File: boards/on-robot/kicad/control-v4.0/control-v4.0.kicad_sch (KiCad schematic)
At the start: 7 parts, among them IC1 MCP23017E_SS, J1 Conn_01x08_MountingPin, U1 Teensy4.1, U3 NRF24L01_Breakout

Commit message: 10/8
Update 10/8
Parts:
- removed J1: Conn_01x08_MountingPin, Connector_JST:JST_SH_SM08B-SRSS-TB_1x08-1MP_P1.00mm_Horizontal, symbol Connector_Generic_MountingPin:Conn_01x08_MountingPin
- added C1: 0.1 uF, Capacitor_SMD:CP_Elec_3x5.3, symbol Device:C_Small
- added J2, J3, J4, J5: 52901-0274, RoboJackets-Connectors:529010274, symbol 52901-0274:52901-0274
- R1: footprint (none) -> Resistor_SMD:R_0201_0603Metric
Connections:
- net RX_M3: now also U1.42 (20_A6_TX5_LRCLK1); no longer U1.36 (14_A0_TX3_SPDIF_OUT)
- net TX_M3: now also U1.43 (21_A7_RX5_BCLK1); no longer U1.37 (15_A1_RX3_SPDIF_IN)
- net GND: now reaches U3.1 (GND)
- net GND: now also IC1.10 (VSS), IC1.15 (A0), IC1.16 (A1), IC1.17 (A2), IC1.18 (/RESET), IC1.9 (VDD), S1.C1, S1.C2, U2.5 (GND), C1.2, J2.12, J2.14, J2.16, J2.18, J2.20, J3.12, J3.14, J3.16, J3.18, J3.20, J4.12, J4.14, J4.16, J4.18, J4.20, J5.12, J5.14, J5.16, J5.18, J5.20
- net +3.3V: now reaches U3.2 (VCC)
- net +3.3V: now also U2.4 (~{CS}), U2.8 (3.3V), U3.4 (~{CSN}), C1.1
- net INT-RAD0: now reaches U3.3 (CE)
- net SCL: now reaches U3.5 (SCK)
- net SDA: now reaches U3.6 (MOSI)
- net SDA: now also IC1.13 (SDA), U2.1 (MOSI)
- net ADDR_IMU: now reaches U3.7 (MISO)
- net ADDR_IMU: now also U2.2 (MISO)
- net SCL-1.2: now reaches IC1.12 (SCK)
- net INT-IO: now reaches IC1.20 (INTA)
- net INT-IO: now also U1.24 (32_OUT1B)
- net HEX-1: now reaches IC1.25 (GPA4)
- net HEX-1: now also S1.2
- net HEX-3: now reaches IC1.26 (GPA5)
- net HEX-3: now also S1.8
- net HEX-2: now reaches IC1.27 (GPA6)
- net HEX-2: now also S1.4
- net HEX-0: now reaches IC1.28 (GPA7)
- net HEX-0: now also S1.1
- net Shared SPI MOSI: now reaches U1.18 (26_A12_MOSI1)
- net Shared SPI MOSI: now also U1.31 (39_MISO1_OUT1A)
- net Shared SPI SCK: now reaches U1.19 (27_A13_SCK1)
- net KICKER SPI MOSI: now reaches U1.2 (0_RX1_CRX2_CS1)
- net INT-IMU: now reaches U1.25 (33_MCLK2)
- net INT-IMU: now also U2.6 (INT)
- net KICKER SPI MISO: now reaches U1.3 (1_TX1_CTX2_MISO1)
- net Shared SPI HW CS: now reaches U1.30 (38_CS1_IN1)
- net RADIO-CE: now reaches U1.33 (41_A17)
- net OLED SCL: now reaches U1.38 (16_A2_RX4_SCL1)
- net OLED SDA: now reaches U1.39 (17_A3_TX4_SDA1)
- net KICKER SPI CSn: now reaches U1.4 (2_OUT2)
- net IMU-SDA: now reaches U1.40 (18_A4_SDA)
- net IMU-SCL: now reaches U1.41 (19_A5_SCL)
- net KICKER SPI RESET: now reaches U1.5 (3_LRCLK2)
- net SCL1.2: now reaches U2.3 (SCK)
- new net +3V3: J2.10, J2.2, J2.4, J2.6, J2.8, J3.10, J3.2, J3.4, J3.6, J3.8, J4.10, J4.2, J4.4, J4.6, J4.8, J5.10, J5.2, J5.4, J5.6, J5.8
- new net DIAG_EN: J3.11
- new net LATCH: J3.15
- new net M1_NRST: J2.5
- new net M1_USART_Rx: J2.3
- new net M1_USART_Tx: J2.1
- new net M2_NRST: J4.5
- new net M2_USART_Rx: J4.3
- new net M2_USART_Tx: J4.1
- new net M3_NRST: J5.5
- new net M3_USART_Rx: J5.3
- new net M3_USART_Tx: J5.1
- new net M4_NRST: J3.5
- new net M4_USART_Rx: J3.3
- new net M4_USART_Tx: J3.1
- new net MISO_KICK: J2.7
- new net MOSI_KICK: J2.9
- new net Radio CSN: U1.36 (14_A0_TX3_SPDIF_OUT)
- new net Radio Interrupt: U1.37 (15_A1_RX3_SPDIF_IN)
- new net SCK_KICK: J2.11
- new net SNS: J3.17
- new net ~{CS}_KICK: J2.13
- new net ~{FAULT}: J3.13
- new net ~{INT}: J3.7
- new net ~{KILL}: J3.9
- new net ~{RST}_KICK: J2.15
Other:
- moved on the sheet: IC1, R1, S1, U1, U2, U3

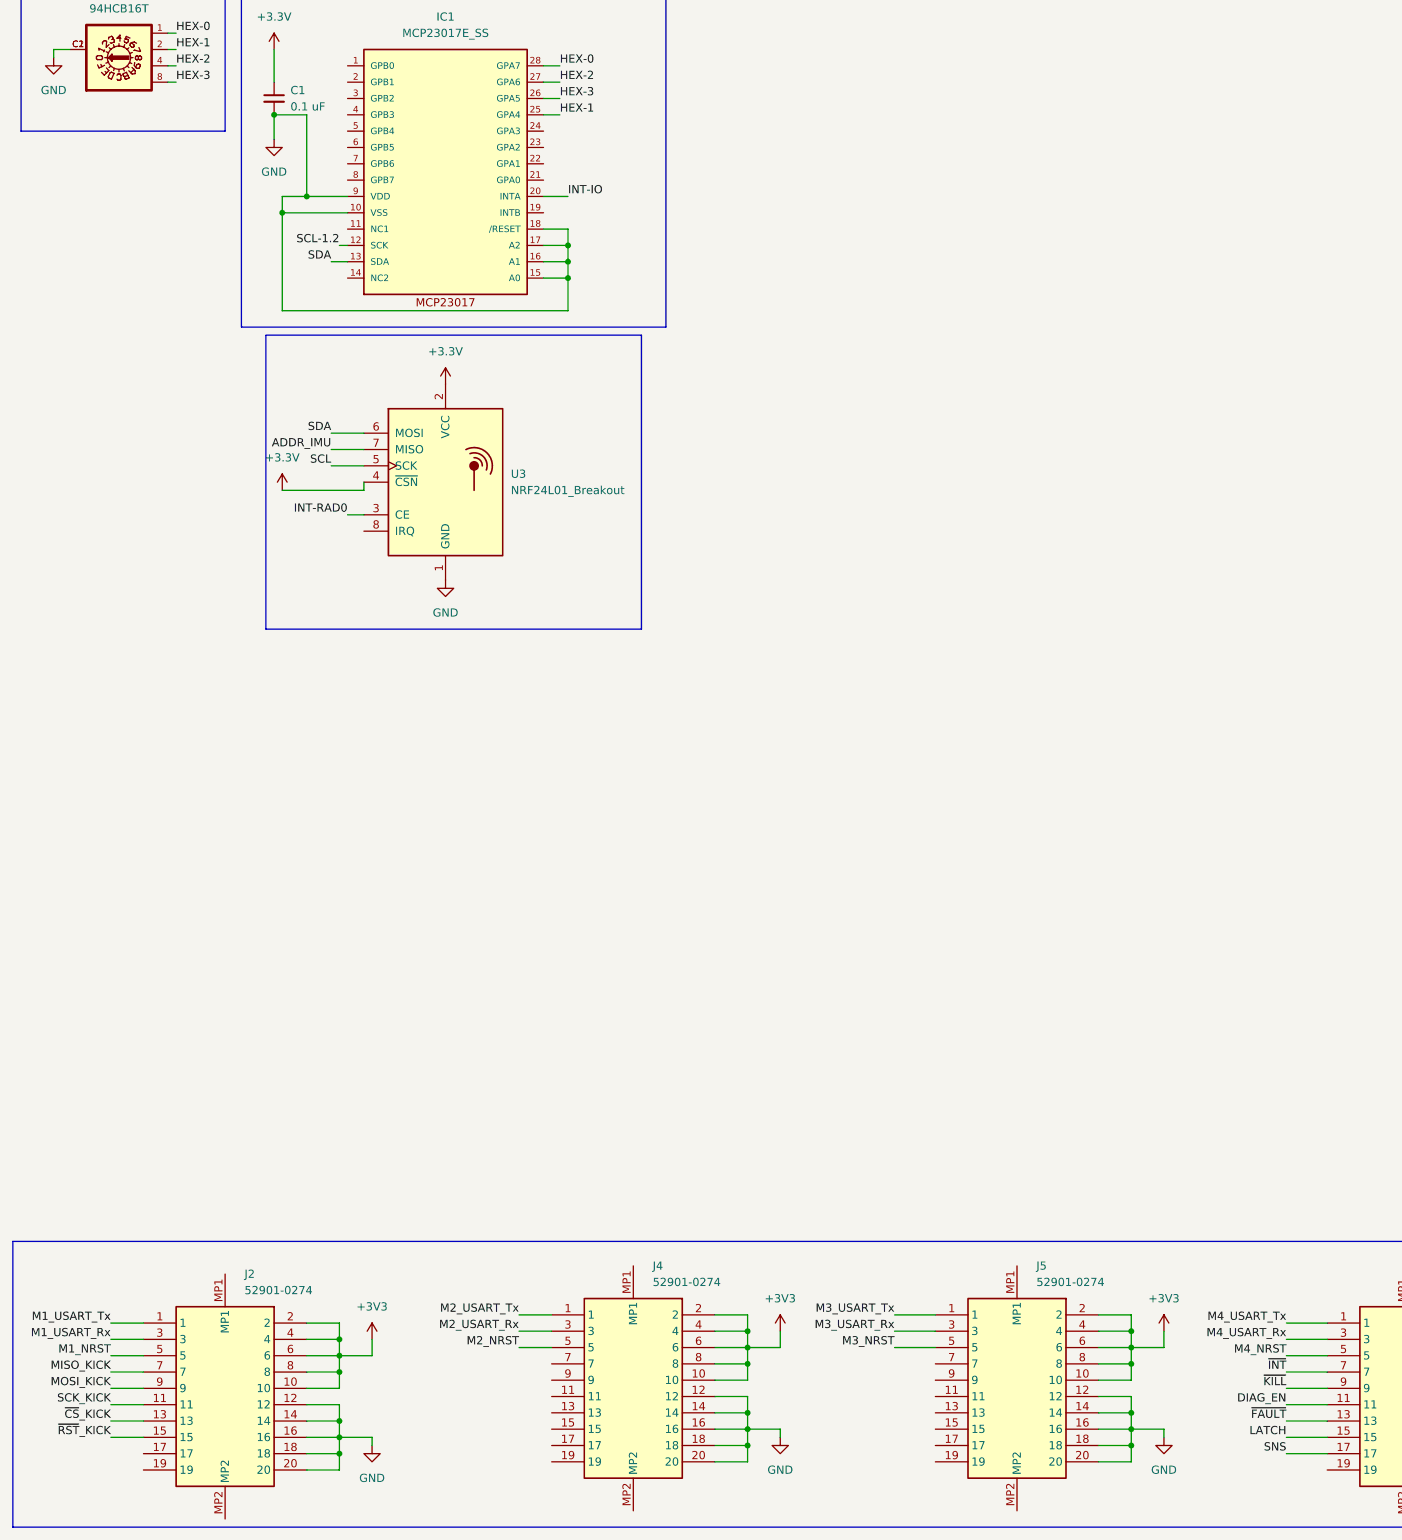
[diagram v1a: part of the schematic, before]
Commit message: Added motor prog to pinout
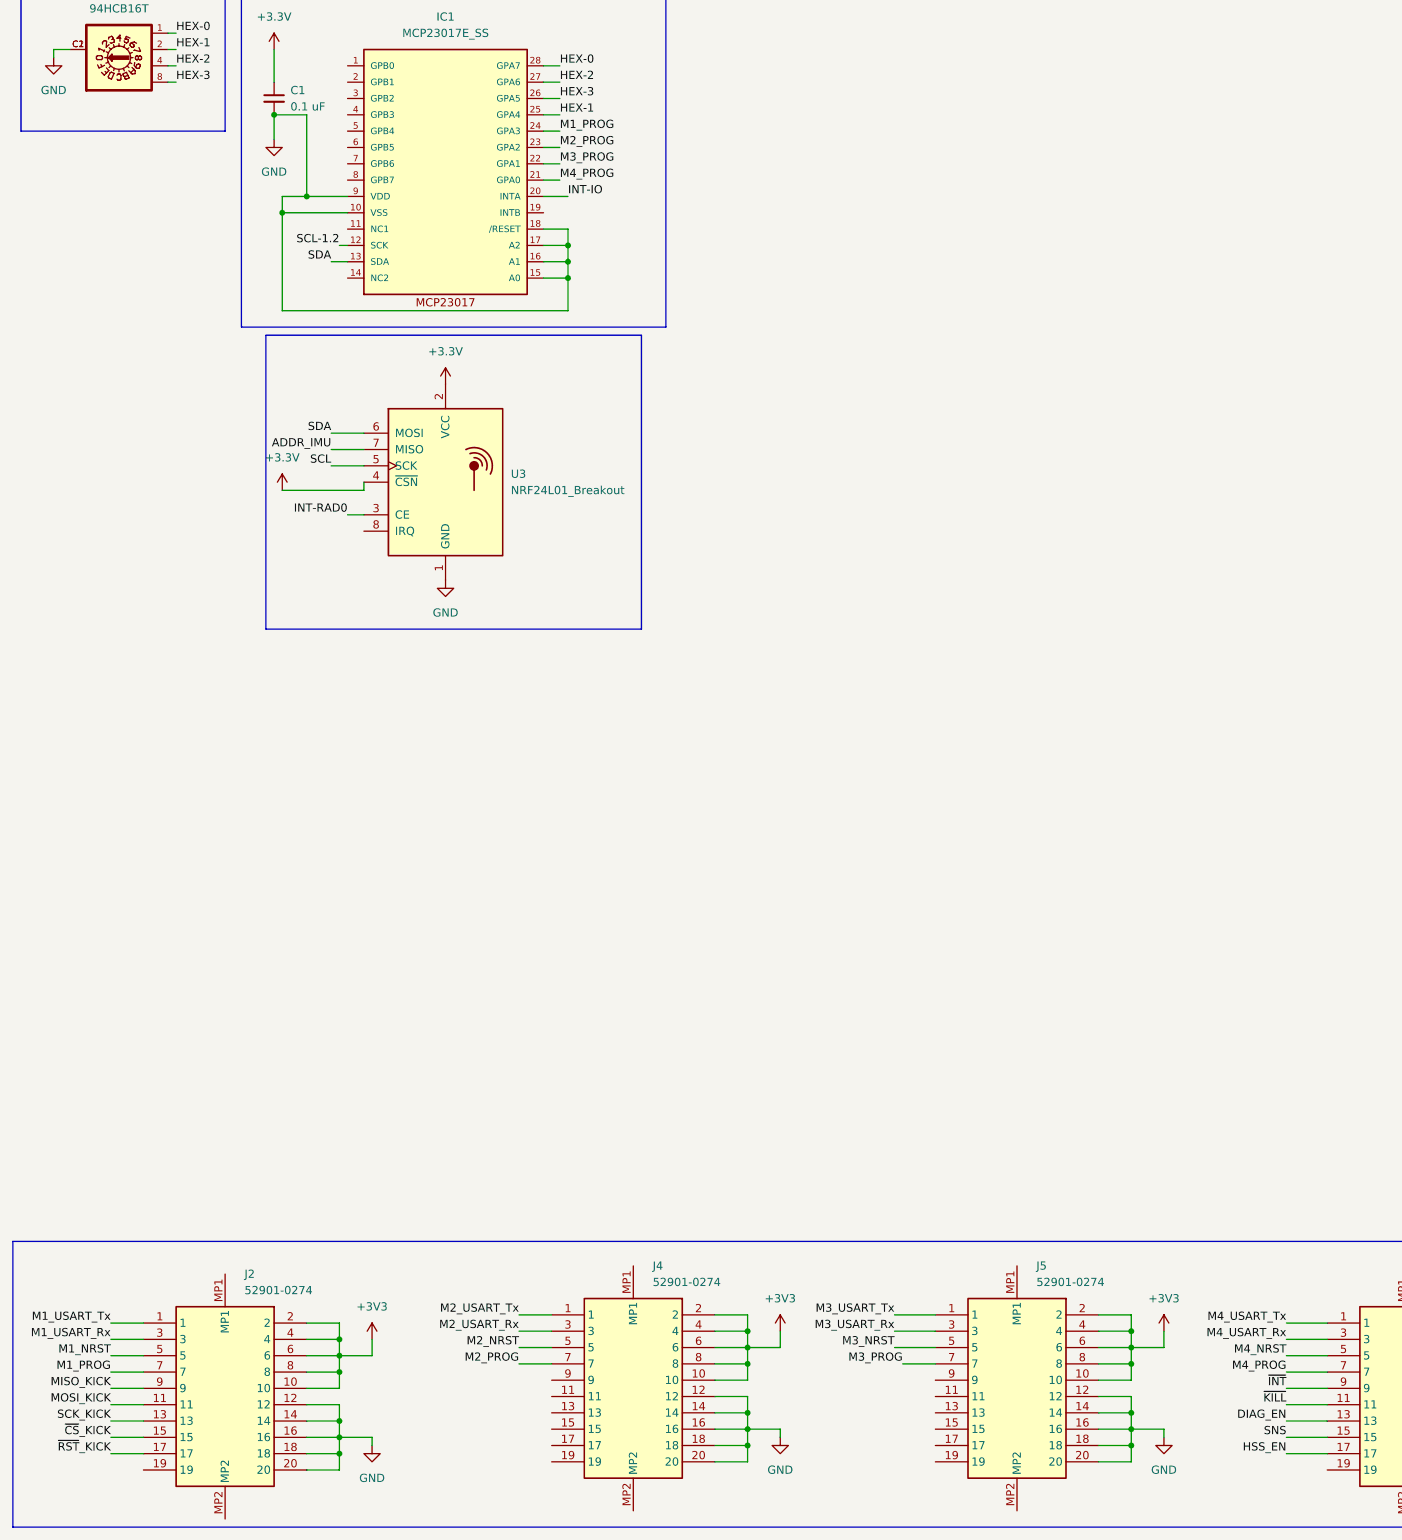
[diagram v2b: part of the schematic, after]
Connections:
- net LATCH is gone; now on net SNS: J3.15
- net ~{FAULT} is gone; now on net DIAG_EN: J3.13
- net DIAG_EN: no longer J3.11
- net MISO_KICK: now also J2.9; no longer J2.7
- net MOSI_KICK: now also J2.11; no longer J2.9
- net SCK_KICK: now also J2.13; no longer J2.11
- net SNS: no longer J3.17
- net ~{CS}_KICK: now also J2.15; no longer J2.13
- net ~{INT}: now also J3.9; no longer J3.7
- net ~{KILL}: now also J3.11; no longer J3.9
- net ~{RST}_KICK: now also J2.17; no longer J2.15
- net M2_PROG: now reaches J4.7
- net M2_PROG: now also IC1.23 (GPA2)
- net M4_PROG: now reaches IC1.21 (GPA0)
- net M4_PROG: now also J3.7
- net M3_PROG: now reaches IC1.22 (GPA1)
- net M3_PROG: now also J5.7
- net M1_PROG: now reaches IC1.24 (GPA3)
- net M1_PROG: now also J2.7
- new net HSS_EN: J3.17

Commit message: Revert "Added motor prog to pinout"
This reverts commit 63edc274fb6eba9204481b3db4263262716e4a11.
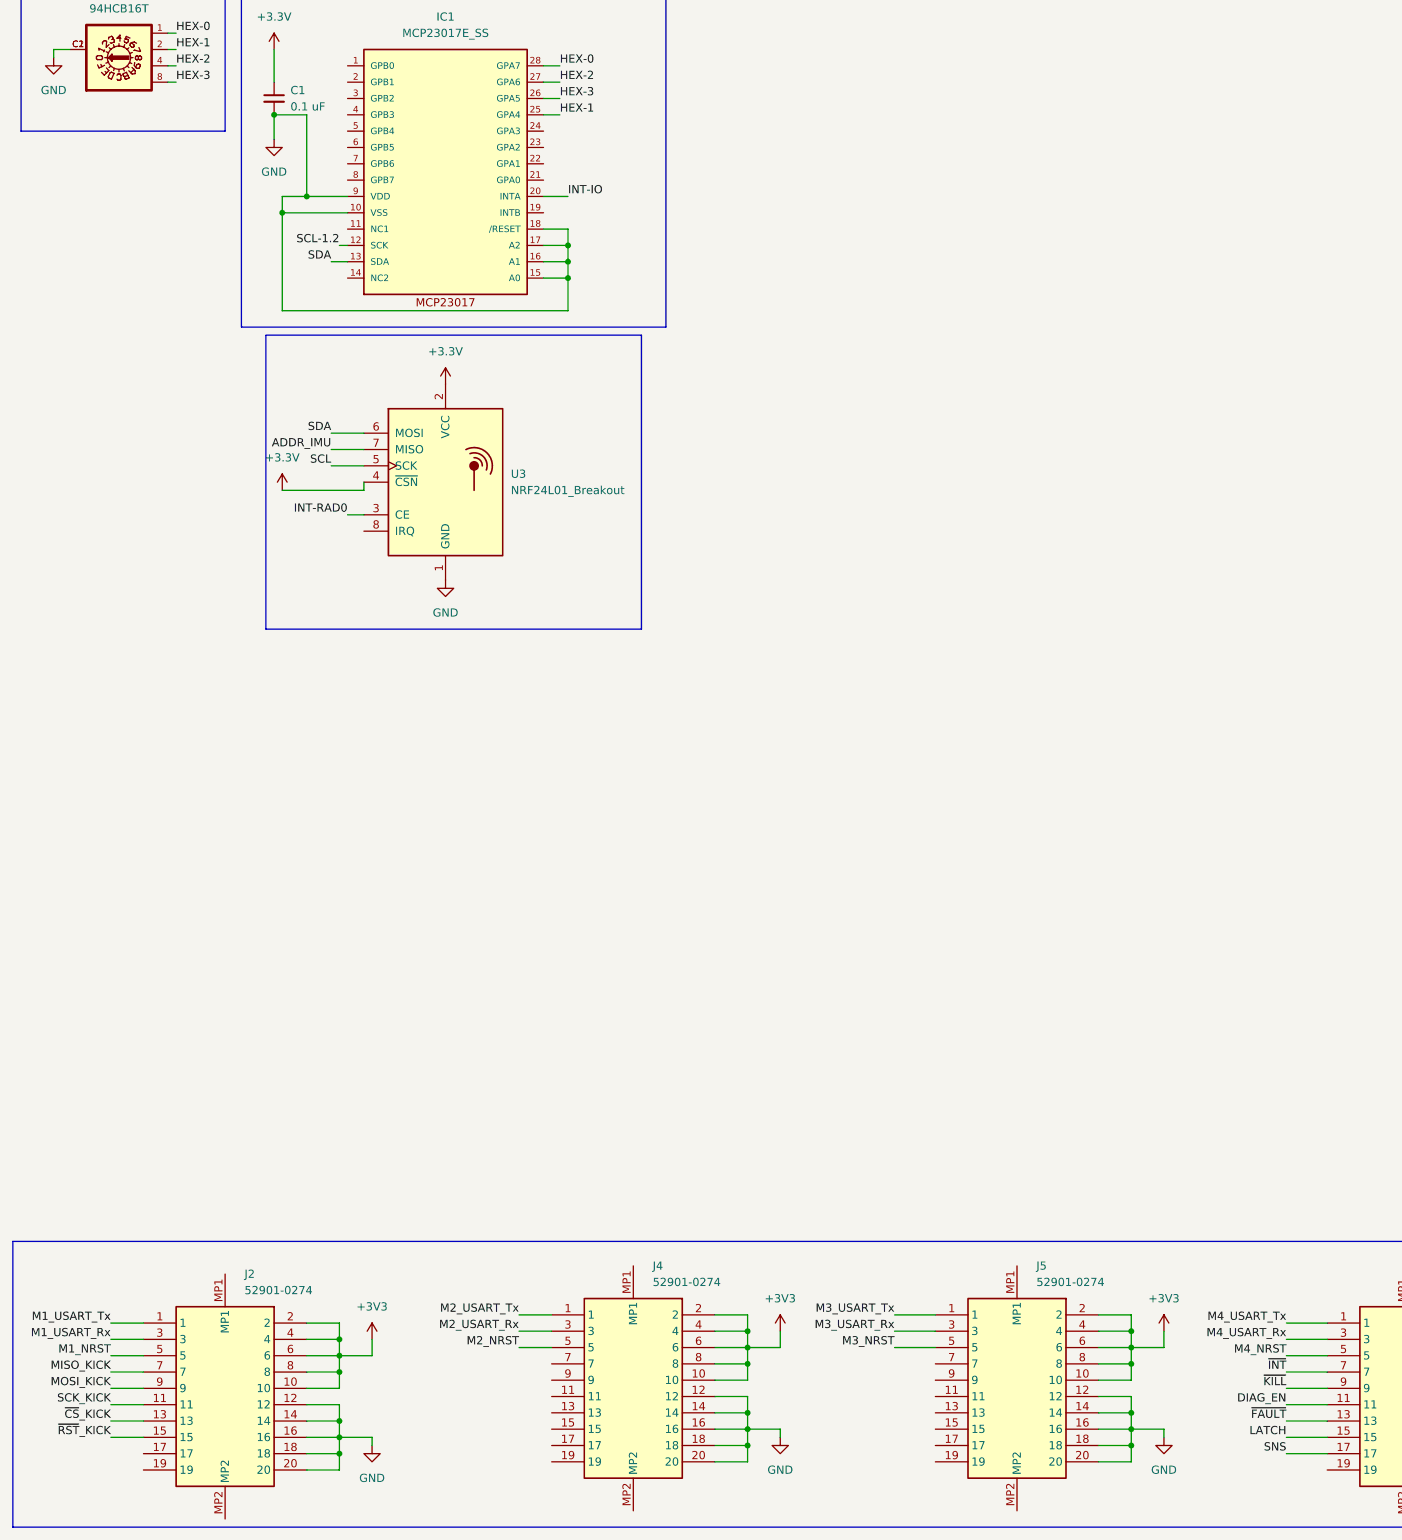
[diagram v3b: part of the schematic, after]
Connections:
- net HSS_EN is gone; now on net SNS: J3.17
- net DIAG_EN: now also J3.11; no longer J3.13
- net MISO_KICK: now also J2.7; no longer J2.9
- net MOSI_KICK: now also J2.9; no longer J2.11
- net SCK_KICK: now also J2.11; no longer J2.13
- net SNS: no longer J3.15
- net ~{CS}_KICK: now also J2.13; no longer J2.15
- net ~{INT}: now also J3.7; no longer J3.9
- net ~{KILL}: now also J3.9; no longer J3.11
- net ~{RST}_KICK: now also J2.15; no longer J2.17
- net M1_PROG: no longer names the net of IC1.24 (GPA3)
- net M1_PROG: no longer J2.7
- net M2_PROG: no longer names the net of J4.7
- net M2_PROG: no longer IC1.23 (GPA2)
- net M3_PROG: no longer names the net of IC1.22 (GPA1)
- net M3_PROG: no longer J5.7
- net M4_PROG: no longer names the net of IC1.21 (GPA0)
- net M4_PROG: no longer J3.7
- new net LATCH: J3.15
- new net ~{FAULT}: J3.13

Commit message: Review Edits 10/20
Changed Label Names Motorboard-Connector Parts
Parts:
- removed J2, J3, J4, J5: 52901-0274, RoboJackets-Connectors:529010274, symbol 52901-0274:52901-0274
- added J1, J6, J7, J8: 53625-0274, RoboJackets-Connectors:536250274, symbol RoboJackets-Connectors:53625-0274
- added R2: 10k, Resistor_SMD:R_0201_0603Metric, symbol Device:R_Small_US
- R1: value R_Small_US -> 10k
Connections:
- net IMU-SDA is gone; now on net IMU_SDA: U1.40 (18_A4_SDA)
- net Radio Interrupt is gone; now on net RADIO_INT: U1.37 (15_A1_RX3_SPDIF_IN)
- net SCL-1.2 is gone; now on net SHARE_SCL: IC1.12 (SCK)
- net SCL1.2 is gone; now on net IMU_SCL: U2.3 (SCK)
- net +3.3V: now also R1.1, U1.48 (VIN), R2.1
- net +3V3: now also J6.10, J6.2, J6.4, J6.6, J6.8, J7.10, J7.2, J7.4, J7.6, J7.8
- net GND: now also U1.1 (GND), U1.34 (GND), U1.47 (GND), U1.52 (GND), U1.58 (GND), U1.59 (GND), U1.64 (GND), J1.12, J1.14, J1.16, J1.18, J1.20, J6.12, J6.14, J6.16, J6.18, J6.20, J7.12, J7.14, J7.16, J7.18, J7.20, J8.12, J8.14, J8.16, J8.18, J8.20
- net MISO_KICK: now also J6.9
- net MOSI_KICK: now also J6.11
- net SCK_KICK: now also J6.13
- net SNS: now also J8.15
- net ~{CS}_KICK: now also J6.15
- net ~{INT}: now also J8.9
- net ~{KILL}: now also J8.11
- net ~{RST}_KICK: now also J6.17
- net IMU_SDA: now reaches R1.2
- net IMU_SDA: now also U2.1 (MOSI)
- net M1_PROG: now reaches IC1.1 (GPB0)
- net M1_PROG: now also J1.7
- net M2_PROG: now reaches IC1.2 (GPB1)
- net M2_PROG: now also J6.7
- net M3_PROG: now reaches IC1.3 (GPB2)
- net M3_PROG: now also J7.7
- net M4_PROG: now reaches IC1.4 (GPB3)
- net M4_PROG: now also J8.7
- net DRIB_PROG: now reaches IC1.5 (GPB4)
- net DRIB_PROG: now also J1.15
- net DRIB_UART_RX: now reaches U1.10 (8_TX2_IN1)
- net RADIO_MOSI: now reaches U1.13 (11_MOSI_CTX1)
- net RADIO_MISO: now reaches U1.14 (12_MISO_MQSL)
- net RADIO_SCK: now reaches U1.35 (13_SCK_LED)
- net DRIB_UART_TX: now reaches U1.9 (7_RX2_OUT1A)
- net HEX-0 renamed HEX_0
- net HEX-1 renamed HEX_1
- net HEX-2 renamed HEX_2
- net HEX-3 renamed HEX_3
- net IMU-SCL renamed IMU_SCL
- net IMU_SCL: now also R2.2
- net INT-IMU renamed INT_IMU
- net INT-IO renamed INT_IO
- net INT-RAD0 renamed RADIO_INT
- net KICKER SPI CSn renamed ~{KICK_CS}
- net KICKER SPI MISO renamed KICK_MISO
- net KICKER SPI MOSI renamed KICK_MOSI
- net KICKER SPI RESET renamed KICK_RESET
- net OLED SCL renamed SHARE_SCL
- net OLED SDA renamed SHARE_SDA
- net SHARE_SDA: now also IC1.13 (SDA)
- net RADIO-CE renamed RADIO_CE
- net Radio CSN renamed ~{RADIO_CS}
- net SCL renamed RADIO_SCL
- removed net SDA: IC1.13 (SDA), U2.1 (MOSI), U3.6 (MOSI)
- net Shared SPI HW CS: no longer names the net of U1.30 (38_CS1_IN1)
- net Shared SPI MOSI: no longer names the net of U1.18 (26_A12_MOSI1)
- net Shared SPI MOSI: no longer U1.31 (39_MISO1_OUT1A)
- net Shared SPI SCK: no longer names the net of U1.19 (27_A13_SCK1)
- new net +5V: J1.10, J1.2, J1.4, J1.6, J1.8, J8.10, J8.2, J8.4, J8.6, J8.8
- new net DIAG_EM: J8.13
- new net DRIB_NRST: J1.13
- new net DRIB_UART_Rx: J1.11
- new net DRIB_UART_Tx: J1.9
- new net HS_EM: J8.17
- new net M1_UART_Rx: J1.3
- new net M1_UART_Tx: J1.1
- new net M2_UART_Rx: J6.3
- new net M2_UART_Tx: J6.1
- new net M3_UART_Rx: J7.3
- new net M3_UART_Tx: J7.1
- new net M4_UART_Rx: J8.3
- new net M4_UART_Tx: J8.1
- new net RADIO_SDA: U3.6 (MOSI)
- new net ~{M1_RST}: J1.5
- new net ~{M2_RST}: J6.5
- new net ~{M3_RST}: J7.5
- new net ~{M4_RST}: J8.5
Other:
- moved on the sheet: C1, IC1, R1, U1, U2

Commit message: 10/20
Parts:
- added Brd1: SSD1306, SSD1306:128x64OLED, symbol SSD1306-128x64_OLED:SSD1306
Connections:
- net +5V: now also Brd1.2 (VCC)
- net GND: now also Brd1.1 (GND)
- net SHARE_SCL: now also Brd1.3 (SCL)
- net SHARE_SDA: now also Brd1.4 (SDA)
